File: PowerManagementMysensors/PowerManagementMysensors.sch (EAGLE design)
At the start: 51 parts, among them IC2 AT25DF512C-SSHN-B, U1 LM8364BALMF20, U2 SI2399DS-T1-GE3, U3 SI2399DS-T1-GE3, U4 MCP1640BT-I/CHY, U5 TPS61222DCKT

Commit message: jst connector added
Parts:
- BATT: value M02PTH -> (none); device SparkFun-Connectors:M02PTH -> adafruit:JST_2PIN-THM
- J10: device SparkFun-Connectors:M05PTH -> SparkFun-Connectors:M04PTH
- J7: device SparkFun-Connectors:M07 -> SparkFun-Connectors:M05PTH
- J8: device SparkFun-Connectors:M04PTH -> SparkFun-Connectors:M05PTH
- J9: device SparkFun-Connectors:M05PTH -> SparkFun-Connectors:M07
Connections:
- net GND: now also BATT.1, J7.3, J9.5; no longer BATT.2, J7.5, J9.3
- net INT1: now also J10.4; no longer J3.4
- net INT2: now also J3.4; no longer J8.4
- net MISO: now also J9.4; no longer J7.4
- net MOSI: now also J9.3; no longer J7.3
- net SCK: now also J9.2; no longer J7.2
- net SCL: now also J7.1, J8.1; no longer J10.1, J9.1
- net SDA: now also J7.2, J8.2; no longer J10.2, J9.2
- net SPI_CSN: now also J9.1; no longer J7.1
- net V+5: now also J10.1, J7.5, J8.5, J9.7; no longer J10.5, J7.7, J8.1, J9.5
- net VCC_SENSORS: now also J10.2, J7.4, J8.4, J9.6; no longer J10.4, J7.6, J8.2, J9.4
- net VIN: now also BATT.2; no longer BATT.1
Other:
- note added: "Connectors : +3V Sensors +5V GND J1 : free. connected to TX J2 : free. connected to RX J3 : free. connected to D3 INT2 (jumper config) J4 : free. connected to D6. PWM J5 : free. connected to A6. ADC1 J6 : free. connected to A7. ADC2 J7 : I2C1 J8 : I2C2 J9 : free. SPI CSN. connected to D7. J10 : free. connected to D2. INT1 (jumper config)"
- moved on the sheet: BATT, J3

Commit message: changes
-res + zener to flash mem avoid fry
- dual schottky instead two single
- minor component ref changes
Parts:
- removed D4, D5: RB520S30T1G, diode:DIODE-SOD523
- added D2: LL103A-GS08TR-ND, semicon-smd-ipc:D-SOD-80
- added D6: BAT54C, zetex:D_2ASOT23
- added R10: 47r-100r, SparkFun-Passives:RESISTOR1206
- D1: value RB520S30T1G -> LL103A-GS08TR-ND; device diode:DIODE-SOD523 -> semicon-smd-ipc:D-SOD-80
- D3: value RB520S30T1G -> BZT52H-B3V6; device diode:DIODE-SOD523 -> adafruit:DIODESOD-123
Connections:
- new net D5_ENBOOST: APM.5, D6.A2
- net EN_BOOST: now also D6.C; no longer D1.C, D3.C
- net EN_POWER: now also D1.C; no longer D5.C
- net EN_POWERRF: now also D2.C; no longer D4.C
- net GND: now also D3.A
- net N$5: now also D6.A1; no longer D3.A
- net N$6: now also D3.C, IC2.!HOLD, IC2.!WP, IC2.VCC, R10.1; no longer APM.5, D1.A
- net VCC: now also D1.A, D2.A, R10.2; no longer D4.A, D5.A, IC2.!HOLD, IC2.!WP, IC2.VCC
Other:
- moved on the sheet: AVRSPI, D1, D3, IC2

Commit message: silkscreen changed, Bom added
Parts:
- L1, L2: device SparkFun-Passives:INDUCTOR1210 -> SparkFun-Passives:INDUCTOR0805
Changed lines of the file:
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@@
 <grid distance="0.1" unitdist="inch" unit="inch" style="lines" multiple="1" display="no" altdistance="0.01" altunitdist="inch" altunit="inch"/>
 <layers>
-<layer number="1" name="Top" color="4" fill="1" visible="no" active="no"/>
-<layer number="2" name="Route2" color="1" fill="3" visible="no" active="no"/>
-<layer number="3" name="Route3" color="4" fill="3" visible="no" active="no"/>
-<layer number="4" name="Route4" color="1" fill="4" visible="no" active="no"/>
-<layer number="5" name="Route5" color="4" fill="4" visible="no" active="no"/>
-<layer number="6" name="Route6" color="1" fill="8" visible="no" active="no"/>
-<layer number="7" name="Route7" color="4" fill="8" visible="no" active="no"/>
-<layer number="8" name="Route8" color="1" fill="2" visible="no" active="no"/>
-<layer number="9" name="Route9" color="4" fill="2" visible="no" active="no"/>
-<layer number="10" name="Route10" color="1" fill="7" visible="no" active="no"/>
-<layer number="11" name="Route11" color="4" fill="7" visible="no" active="no"/>
-<layer number="12" name="Route12" color="1" fill="5" visible="no" active="no"/>
-<layer number="13" name="Route13" color="4" fill="5" visible="no" active="no"/>
-<layer number="14" name="Route14" color="1" fill="6" visible="no" active="no"/>
-<layer number="15" name="Route15" color="4" fill="6" visible="no" active="no"/>
-<layer number="16" name="Bottom" color="1" fill="1" visible="no" active="no"/>
-<layer number="17" name="Pads" color="2" fill="1" visible="no" active="no"/>
-<layer number="18" name="Vias" color="2" fill="1" visible="no" active="no"/>
-<layer number="19" name="Unrouted" color="6" fill="1" visible="no" active="no"/>
-<layer number="20" name="Dimension" color="15" fill="1" visible="no" active="no"/>
-<layer number="21" name="tPlace" color="7" fill="1" visible="no" active="no"/>
-<layer number="22" name="bPlace" color="7" fill="1" visible="no" active="no"/>
-<layer number="23" name="tOrigins" color="15" fill="1" visible="no" active="no"/>
-<layer number="24" name="bOrigins" color="15" fill="1" visible="no" active="no"/>
-<layer number="25" name="tNames" color="7" fill="1" visible="no" active="no"/>
-<layer number="26" name="bNames" color="7" fill="1" visible="no" active="no"/>
-<layer number="27" name="tValues" color="7" fill="1" visible="no" active="no"/>
-<layer number="28" name="bValues" color="7" fill="1" visible="no" active="no"/>
+<layer number="1" name="Top" color="4" fill="1" visible="yes" active="no"/>
+<layer number="2" name="Route2" color="1" fill="3" visible="yes" active="no"/>
+<layer number="3" name="Route3" color="4" fill="3" visible="yes" active="no"/>
+<layer number="4" name="Route4" color="1" fill="4" visible="yes" active="no"/>
+<layer number="5" name="Route5" color="4" fill="4" visible="yes" active="no"/>
+<layer number="6" name="Route6" color="1" fill="8" visible="yes" active="no"/>
+<layer number="7" name="Route7" color="4" fill="8" visible="yes" active="no"/>
+<layer number="8" name="Route8" color="1" fill="2" visible="yes" active="no"/>
+<layer number="9" name="Route9" color="4" fill="2" visible="yes" active="no"/>
+<layer number="10" name="Route10" color="1" fill="7" visible="yes" active="no"/>
+<layer number="11" name="Route11" color="4" fill="7" visible="yes" active="no"/>
+<layer number="12" name="Route12" color="1" fill="5" visible="yes" active="no"/>
+<layer number="13" name="Route13" color="4" fill="5" visible="yes" active="no"/>
+<layer number="14" name="Route14" color="1" fill="6" visible="yes" active="no"/>
+<layer number="15" name="Route15" color="4" fill="6" visible="yes" active="no"/>
+<layer number="16" name="Bottom" color="1" fill="1" visible="yes" active="no"/>
+<layer number="17" name="Pads" color="2" fill="1" visible="yes" active="no"/>
+<layer number="18" name="Vias" color="2" fill="1" visible="yes" active="no"/>
+<layer number="19" name="Unrouted" color="6" fill="1" visible="yes" active="no"/>
+<layer number="20" name="Dimension" color="15" fill="1" visible="yes" active="no"/>
+<layer number="21" name="tPlace" color="7" fill="1" visible="yes" active="no"/>
+<layer number="22" name="bPlace" color="7" fill="1" visible="yes" active="no"/>
+<layer number="23" name="tOrigins" color="15" fill="1" visible="yes" active="no"/>
+<layer number="24" name="bOrigins" color="15" fill="1" visible="yes" active="no"/>
+<layer number="25" name="tNames" color="7" fill="1" visible="yes" active="no"/>
+<layer number="26" name="bNames" color="7" fill="1" visible="yes" active="no"/>
+<layer number="27" name="tValues" color="7" fill="1" visible="yes" active="no"/>
+<layer number="28" name="bValues" color="7" fill="1" visible="yes" active="no"/>
 <layer number="29" name="tStop" color="7" fill="3" visible="no" active="no"/>
 <layer number="30" name="bStop" color="7" fill="6" visible="no" active="no"/>
@@
 <layer number="35" name="tGlue" color="7" fill="4" visible="no" active="no"/>
 <layer number="36" name="bGlue" color="7" fill="5" visible="no" active="no"/>
-<layer number="37" name="tTest" color="7" fill="1" visible="no" active="no"/>
-<layer number="38" name="bTest" color="7" fill="1" visible="no" active="no"/>
+<layer number="37" name="tTest" color="7" fill="1" visible="yes" active="no"/>
+<layer number="38" name="bTest" color="7" fill="1" visible="yes" active="no"/>
 <layer number="39" name="tKeepout" color="4" fill="11" visible="no" active="no"/>
 <layer number="40" name="bKeepout" color="1" fill="11" visible="no" active="no"/>
@@
 <layer number="44" name="Drills" color="7" fill="1" visible="no" active="no"/>
 <layer number="45" name="Holes" color="7" fill="1" visible="no" active="no"/>
-<layer number="46" name="Milling" color="3" fill="1" visible="no" active="no"/>
-<layer number="47" name="Measures" color="7" fill="1" visible="no" active="no"/>
-<layer number="48" name="Document" color="7" fill="1" visible="no" active="no"/>
-<layer number="49" name="Reference" color="7" fill="1" visible="no" active="no"/>
-<layer number="50" name="dxf" color="7" fill="1" visible="no" active="no"/>
-<layer number="51" name="tDocu" color="7" fill="1" visible="no" active="no"/>
-<layer number="52" name="bDocu" color="7" fill="1" visible="no" active="no"/>
-<layer number="53" name="tGND_GNDA" color="7" fill="9" visible="no" active="no"/>
-<layer number="54" name="bGND_GNDA" color="1" fill="9" visible="no" active="no"/>
-<layer number="56" name="wert" color="7" fill="1" visible="no" active="no"/>
-<layer number="57" name="tCAD" color="7" fill="1" visible="no" active="no"/>
+<layer number="46" name="Milling" color="3" fill="1" visible="yes" active="no"/>
+<layer number="47" name="Measures" color="7" fill="1" visible="yes" active="no"/>
+<layer number="48" name="Document" color="7" fill="1" visible="yes" active="no"/>
+<layer number="49" name="Reference" color="7" fill="1" visible="yes" active="no"/>
+<layer number="50" name="dxf" color="7" fill="1" visible="yes" active="no"/>
+<layer number="51" name="tDocu" color="7" fill="1" visible="yes" active="no"/>
+<layer number="52" name="bDocu" color="7" fill="1" visible="yes" active="no"/>
+<layer number="53" name="tGND_GNDA" color="7" fill="9" visible="yes" active="no"/>
+<layer number="54" name="bGND_GNDA" color="1" fill="9" visible="yes" active="no"/>
+<layer number="56" name="wert" color="7" fill="1" visible="yes" active="no"/>
+<layer number="57" name="tCAD" color="7" fill="1" visible="yes" active="no"/>
 <layer number="90" name="Modules" color="5" fill="1" visible="yes" active="yes"/>
 <layer number="91" name="Nets" color="2" fill="1" visible="yes" active="yes"/>
@@
 <parts>
 <part name="U4" library="pmo_lib" deviceset="MCP1640BT-I/CHY" device=""/>
-<part name="L1" library="SparkFun-Passives" deviceset="INDUCTOR" device="1210" value="4.7uH"/>
+<part name="L1" library="SparkFun-Passives" deviceset="INDUCTOR" device="0805" value="4.7uH"/>
 <part name="R1" library="SparkFun-Passives" deviceset="RESISTOR" device="1206" value="976k"/>
 <part name="R2" library="SparkFun-Passives" deviceset="RESISTOR" device="1206" value="562k"/>
@@
 <part name="JP4" library="SparkFun-Passives" deviceset="JUMPER-2" device="PTH"/>
 <part name="U5" library="pmo_lib" deviceset="TPS61222DCKT" device=""/>
-<part name="L2" library="SparkFun-Passives" deviceset="INDUCTOR" device="1210" value="4.7uH"/>
+<part name="L2" library="SparkFun-Passives" deviceset="INDUCTOR" device="0805" value="4.7uH"/>
 <part name="C2" library="SparkFun-Passives" deviceset="CAP" device="1206" value="10u"/>
 <part name="C3" library="SparkFun-Passives" deviceset="CAP" device="1206" value="10u"/>

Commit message: gnd plane modified for nrf24
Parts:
- J1, J10, J2, J3, J4, J5, J6: device SparkFun-Connectors:M04PTH -> SparkFun-Connectors:M041X04_NO_SILK
- J7, J8: device SparkFun-Connectors:M05PTH -> SparkFun-Connectors:M05NO_SILK

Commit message: Mosfet + Pull up on LM8364 reset
Pull up on lm8364 was missing. oops. So mosfet and pull up added to
invert signal. Schem changed. Little change for radios gnd plane. BOM
changed
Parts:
- removed U$5: RFM12B_ANTENNA, LowPowerLab:RFM12B_ANTENNA
- added ANT: RFM12B_ANTENNA, LowPowerLab:RFM12B_ANTENNA
- added R11: 10k, SparkFun-Passives:RESISTOR1206
- added U6: BSS123-7-F, pmo_lib:BSS123-7-F
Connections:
- new net N$17: D6.A1, R11.1, U6.D
- net GND: now also U6.S
- net N$2: now also ANT.1; no longer U$5.1
- net N$5: now also U6.G; no longer D6.A1
- net VIN: now also R11.2
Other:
- moved on the sheet: APM, ATSHA, AVRSPI, C12, D1, D2, D3, D6, IC2, J1, J10, J2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

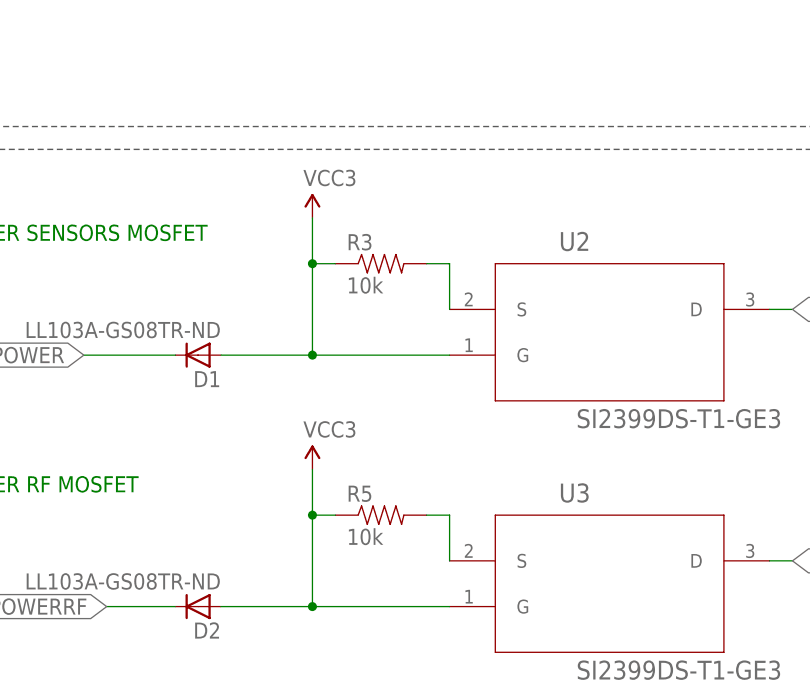
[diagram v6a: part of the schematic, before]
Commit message: change on mosfet power (error in previous version)
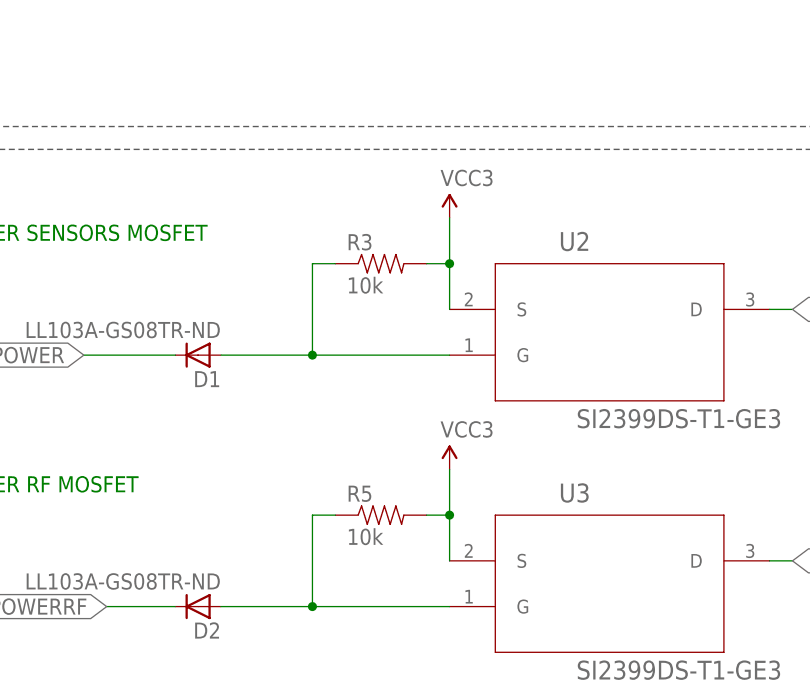
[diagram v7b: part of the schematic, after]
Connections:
- removed net N$3: R3.2, U2.S
- new net N$18: D2.A, R5.1, U3.G
- net N$7: now also D1.A, R3.1, U2.G; no longer R5.2, U3.S
- net VCC: now also R3.2, R5.2, U2.S, U3.S; no longer D1.A, D2.A, R3.1, R5.1, U2.G, U3.G
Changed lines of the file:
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@@
 <instance part="VCC3" gate="G$1" x="86.36" y="99.06"/>
 <instance part="R3" gate="G$1" x="147.32" y="17.78"/>
-<instance part="VCC1" gate="G$1" x="139.7" y="22.86"/>
+<instance part="VCC1" gate="G$1" x="154.94" y="22.86"/>
 <instance part="C1" gate="G$1" x="101.6" y="63.5"/>
 <instance part="U1" gate="A" x="259.08" y="63.5"/>
@@
 <instance part="U2" gate="A" x="154.94" y="12.7"/>
 <instance part="R5" gate="G$1" x="147.32" y="-10.16"/>
-<instance part="VCC5" gate="G$1" x="139.7" y="-5.08"/>
+<instance part="VCC5" gate="G$1" x="154.94" y="-5.08"/>
 <instance part="U3" gate="A" x="154.94" y="-15.24"/>
 <instance part="NRF24" gate="A" x="309.88" y="-10.16"/>
@@
 <net name="VCC" class="0">
 <segment>
-<wire x1="139.7" y1="7.62" x2="139.7" y2="17.78" width="0.1524" layer="91"/>
-<pinref part="R3" gate="G$1" pin="1"/>
-<wire x1="139.7" y1="17.78" x2="142.24" y2="17.78" width="0.1524" layer="91"/>
-<junction x="139.7" y="17.78"/>
-<pinref part="VCC1" gate="G$1" pin="VCC"/>
-<wire x1="139.7" y1="22.86" x2="139.7" y2="17.78" width="0.1524" layer="91"/>
-<pinref part="U2" gate="A" pin="G"/>
-<wire x1="154.94" y1="7.62" x2="139.7" y2="7.62" width="0.1524" layer="91"/>
-<pinref part="D1" gate="G$1" pin="A"/>
-<wire x1="129.54" y1="7.62" x2="139.7" y2="7.62" width="0.1524" layer="91"/>
-<junction x="139.7" y="7.62"/>
-</segment>
-<segment>
 <pinref part="APM" gate="A" pin="VCC"/>
 <pinref part="VCC7" gate="G$1" pin="VCC"/>
@@
 <pinref part="R6" gate="G$1" pin="2"/>
 <wire x1="63.5" y1="-5.08" x2="63.5" y2="0" width="0.1524" layer="91"/>
-</segment>
-<segment>
-<wire x1="139.7" y1="-20.32" x2="139.7" y2="-10.16" width="0.1524" layer="91"/>
-<pinref part="R5" gate="G$1" pin="1"/>
-<wire x1="139.7" y1="-10.16" x2="142.24" y2="-10.16" width="0.1524" layer="91"/>
-<junction x="139.7" y="-10.16"/>
-<pinref part="VCC5" gate="G$1" pin="VCC"/>
-<wire x1="139.7" y1="-5.08" x2="139.7" y2="-10.16" width="0.1524" layer="91"/>
-<pinref part="U3" gate="A" pin="G"/>
-<wire x1="154.94" y1="-20.32" x2="139.7" y2="-20.32" width="0.1524" layer="91"/>
-<pinref part="D2" gate="G$1" pin="A"/>
-<wire x1="129.54" y1="-20.32" x2="139.7" y2="-20.32" width="0.1524" layer="91"/>
-<junction x="139.7" y="-20.32"/>
 </segment>
 <segment>
@@
 <pinref part="VCC8" gate="G$1" pin="VCC"/>
 <wire x1="172.72" y1="-40.64" x2="172.72" y2="-38.1" width="0.1524" layer="91"/>
+</segment>
+<segment>
+<pinref part="R5" gate="G$1" pin="2"/>
+<pinref part="U3" gate="A" pin="S"/>
+<wire x1="152.4" y1="-10.16" x2="154.94" y2="-10.16" width="0.1524" layer="91"/>
+<wire x1="154.94" y1="-10.16" x2="154.94" y2="-15.24" width="0.1524" layer="91"/>
+<junction x="154.94" y="-10.16"/>
+<pinref part="VCC5" gate="G$1" pin="VCC"/>
+<wire x1="154.94" y1="-5.08" x2="154.94" y2="-10.16" width="0.1524" layer="91"/>
+</segment>
+<segment>
+<pinref part="R3" gate="G$1" pin="2"/>
+<pinref part="U2" gate="A" pin="S"/>
+<wire x1="152.4" y1="17.78" x2="154.94" y2="17.78" width="0.1524" layer="91"/>
+<wire x1="154.94" y1="17.78" x2="154.94" y2="12.7" width="0.1524" layer="91"/>
+<junction x="154.94" y="17.78"/>
+<pinref part="VCC1" gate="G$1" pin="VCC"/>
+<wire x1="154.94" y1="22.86" x2="154.94" y2="17.78" width="0.1524" layer="91"/>
 </segment>
 </net>
@@
 </segment>
 </net>
-<net name="N$3" class="0">
-<segment>
-<pinref part="R3" gate="G$1" pin="2"/>
-<pinref part="U2" gate="A" pin="S"/>
-<wire x1="152.4" y1="17.78" x2="154.94" y2="17.78" width="0.1524" layer="91"/>
-<wire x1="154.94" y1="17.78" x2="154.94" y2="12.7" width="0.1524" layer="91"/>
-</segment>
-</net>
-<net name="N$7" class="0">
-<segment>
-<pinref part="R5" gate="G$1" pin="2"/>
-<pinref part="U3" gate="A" pin="S"/>
-<wire x1="152.4" y1="-10.16" x2="154.94" y2="-10.16" width="0.1524" layer="91"/>
-<wire x1="154.94" y1="-10.16" x2="154.94" y2="-15.24" width="0.1524" layer="91"/>
-</segment>
-</net>
 <net name="EN_POWERRF" class="0">
 <segment>
@@
 </segment>
 </net>
+<net name="N$18" class="0">
+<segment>
+<wire x1="139.7" y1="-20.32" x2="139.7" y2="-10.16" width="0.1524" layer="91"/>
+<pinref part="R5" gate="G$1" pin="1"/>
+<wire x1="139.7" y1="-10.16" x2="142.24" y2="-10.16" width="0.1524" layer="91"/>
+<pinref part="U3" gate="A" pin="G"/>
+<wire x1="154.94" y1="-20.32" x2="139.7" y2="-20.32" width="0.1524" layer="91"/>
+<pinref part="D2" gate="G$1" pin="A"/>
+<wire x1="129.54" y1="-20.32" x2="139.7" y2="-20.32" width="0.1524" layer="91"/>
+<junction x="139.7" y="-20.32"/>
+</segment>
+</net>
+<net name="N$7" class="0">
+<segment>
+<wire x1="139.7" y1="7.62" x2="139.7" y2="17.78" width="0.1524" layer="91"/>
+<pinref part="R3" gate="G$1" pin="1"/>
+<wire x1="139.7" y1="17.78" x2="142.24" y2="17.78" width="0.1524" layer="91"/>
+<pinref part="U2" gate="A" pin="G"/>
+<wire x1="154.94" y1="7.62" x2="139.7" y2="7.62" width="0.1524" layer="91"/>
+<pinref part="D1" gate="G$1" pin="A"/>
+<wire x1="129.54" y1="7.62" x2="139.7" y2="7.62" width="0.1524" layer="91"/>
+<junction x="139.7" y="7.62"/>
+</segment>
+</net>

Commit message: Changes in progress, ncp302 added in place of lm834
some files deleted, will be back soon,
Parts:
- removed D6: BAT54C, zetex:D_2ASOT23
- removed U1: LM8364BALMF20, pmo_lib:LM8364BALMF20
- added C4: (no value), SparkFun-Passives:CAP1206
- added U$1: NCP302LSN20T1, pmo_lib:NCP302LSN20T1
- added U7: SI2399DS-T1-GE3, pmo_lib:SI2399DS-T1-GE3
- added VP1, VP2: (no value), wirepad:1,6/0,9
- R4: value 470k -> 4k7
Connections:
- removed net N$17: D6.A1, R11.1, U6.D
- removed net N$5: U1.~RESET, U6.G
- removed net N$9: JP4.1, R4.1, U1.IN
- new net INT_BOOST: JP5.1, U$1.RST, U6.G
- new net N$3: JP4.1, U$1.IN
- new net VBAT: BATT.2, U7.D
- net D5_ENBOOST: now also C4.1, U$1.CD; no longer D6.A2
- net EN_BOOST: now also R11.1, U6.D; no longer D6.C, JP5.1, R4.2
- net GND: now also C4.2, U$1.GND, U7.G; no longer U1.GND
- net PWM: now also R4.1
- net VCC: now also VP1.P, VP2.P
- net VCC_SENSORS: now also R4.2
- net VIN: now also U7.S; no longer BATT.2
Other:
- note added: "Additional VCC3"
- note added: "NRF24 and RFM69 jumper selection"
- note added: "Optional I2C pullups"
- note added: "Optional pullup"
- note added: "Power Input"
- note added: "Reverse polarity protection"
- note added: "or 100o resistor"
- moved on the sheet: APM, AVRSPI, BATT, C1, C12, C2, C3, CIN, COUT, D1, D2, J1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
